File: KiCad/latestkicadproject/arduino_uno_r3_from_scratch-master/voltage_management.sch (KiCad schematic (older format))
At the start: 3 parts, among them U3 LP2985-33DBVR

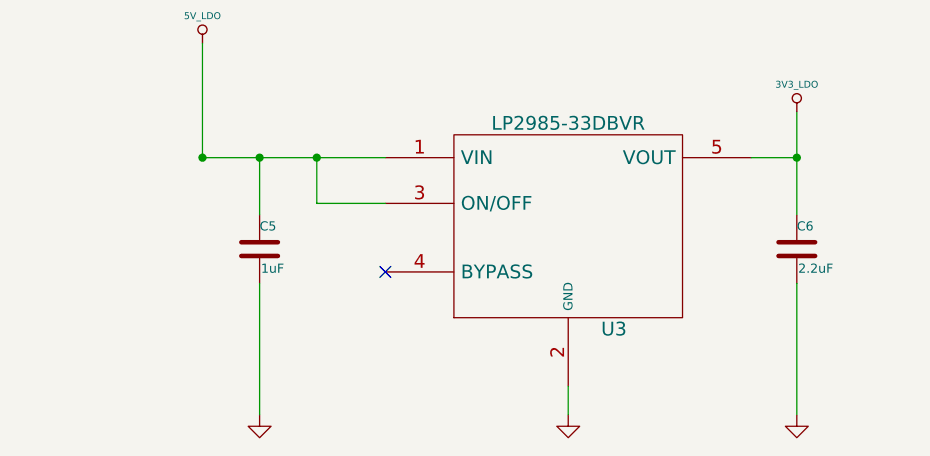
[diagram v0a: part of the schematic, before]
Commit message: 28feb
Aanpassing KiCad+deel footprints
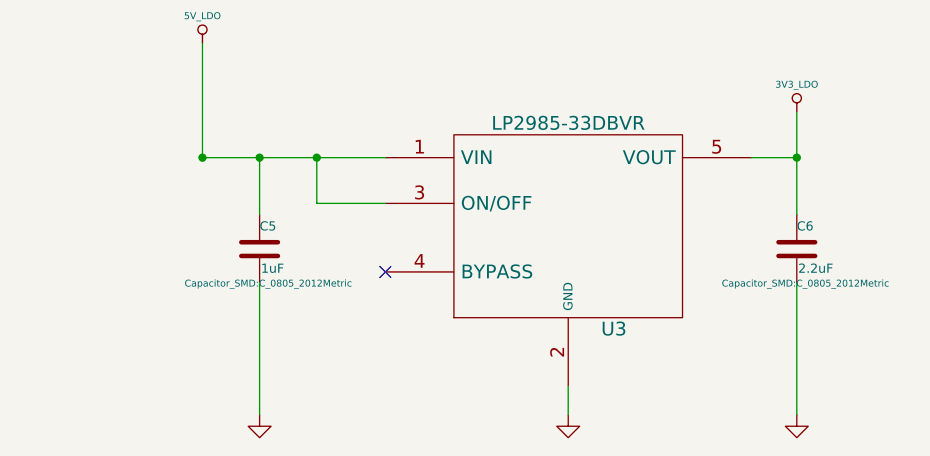
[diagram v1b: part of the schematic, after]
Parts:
- C5, C6: footprint ~ -> Capacitor_SMD:C_0805_2012Metric
- U3: footprint ~ -> (none)
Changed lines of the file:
@@
 F 0 "U3" H 7200 4050 60  0000 C CNN
 F 1 "LP2985-33DBVR" H 7000 4950 60  0000 C CNN
-F 2 "~" H 7000 4500 60  0000 C CNN
+F 2 "" H 7000 4500 60  0000 C CNN
 F 3 "http://www.ti.com/lit/ds/symlink/lp2985-33.pdf" H 7000 4500 60  0001 C CNN
 F 4 "3.3V FIXED POSITIVE LDO REGULATOR, 0.575V DROPOUT" H 7000 4500 60  0001 C CNN "Characteristics"
@@
 F 0 "C6" H 8000 4700 40  0000 L CNN
 F 1 "2.2uF" H 8006 4515 40  0000 L CNN
-F 2 "~" H 8038 4450 30  0000 C CNN
+F 2 "Capacitor_SMD:C_0805_2012Metric" H 8038 4450 30  0000 C CNN
 F 3 "http://product.tdk.com/en/catalog/datasheets/mlcc_commercial_general_en.pdf" H 8000 4600 60  0001 C CNN
 F 4 "CAP CER 2.2UF 16V X7R 0805" H 8000 4600 60  0001 C CNN "Characteristics"
@@
 F 0 "C5" H 5650 4700 40  0000 L CNN
 F 1 "1uF" H 5656 4515 40  0000 L CNN
-F 2 "~" H 5688 4450 30  0000 C CNN
+F 2 "Capacitor_SMD:C_0805_2012Metric" H 5688 4450 30  0000 C CNN
 F 3 "http://www.kemet.com/docfinder?Partnumber=C0805C105K8RACAUTO" H 5650 4600 60  0001 C CNN
 F 4 "CAPACITOR, CERAMIC, MULTILAYER, 10 V, X7R, 1 uF, SURFACE MOUNT, 0805" H 5650 4600 60  0001 C CNN "Characteristics"

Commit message: Toevoegen footprints Kicad
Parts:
- U3: footprint (none) -> LP2985-33DBVR:SOT95P280X145-5N
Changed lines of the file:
@@
 F 0 "U3" H 7200 4050 60  0000 C CNN
 F 1 "LP2985-33DBVR" H 7000 4950 60  0000 C CNN
-F 2 "" H 7000 4500 60  0000 C CNN
+F 2 "LP2985-33DBVR:SOT95P280X145-5N" H 7000 4500 60  0001 C CNN
 F 3 "http://www.ti.com/lit/ds/symlink/lp2985-33.pdf" H 7000 4500 60  0001 C CNN
 F 4 "3.3V FIXED POSITIVE LDO REGULATOR, 0.575V DROPOUT" H 7000 4500 60  0001 C CNN "Characteristics"
